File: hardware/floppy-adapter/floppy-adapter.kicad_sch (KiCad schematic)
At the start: 12 parts, among them J1 Conn_02x17 socket (O1 side), J2 Conn_02x17 header (OEM cable), J3 Conn_02x17 header (Gotek), J4 Gotek power, J5 Panel switch, K1 4PDT relay, 5V coil

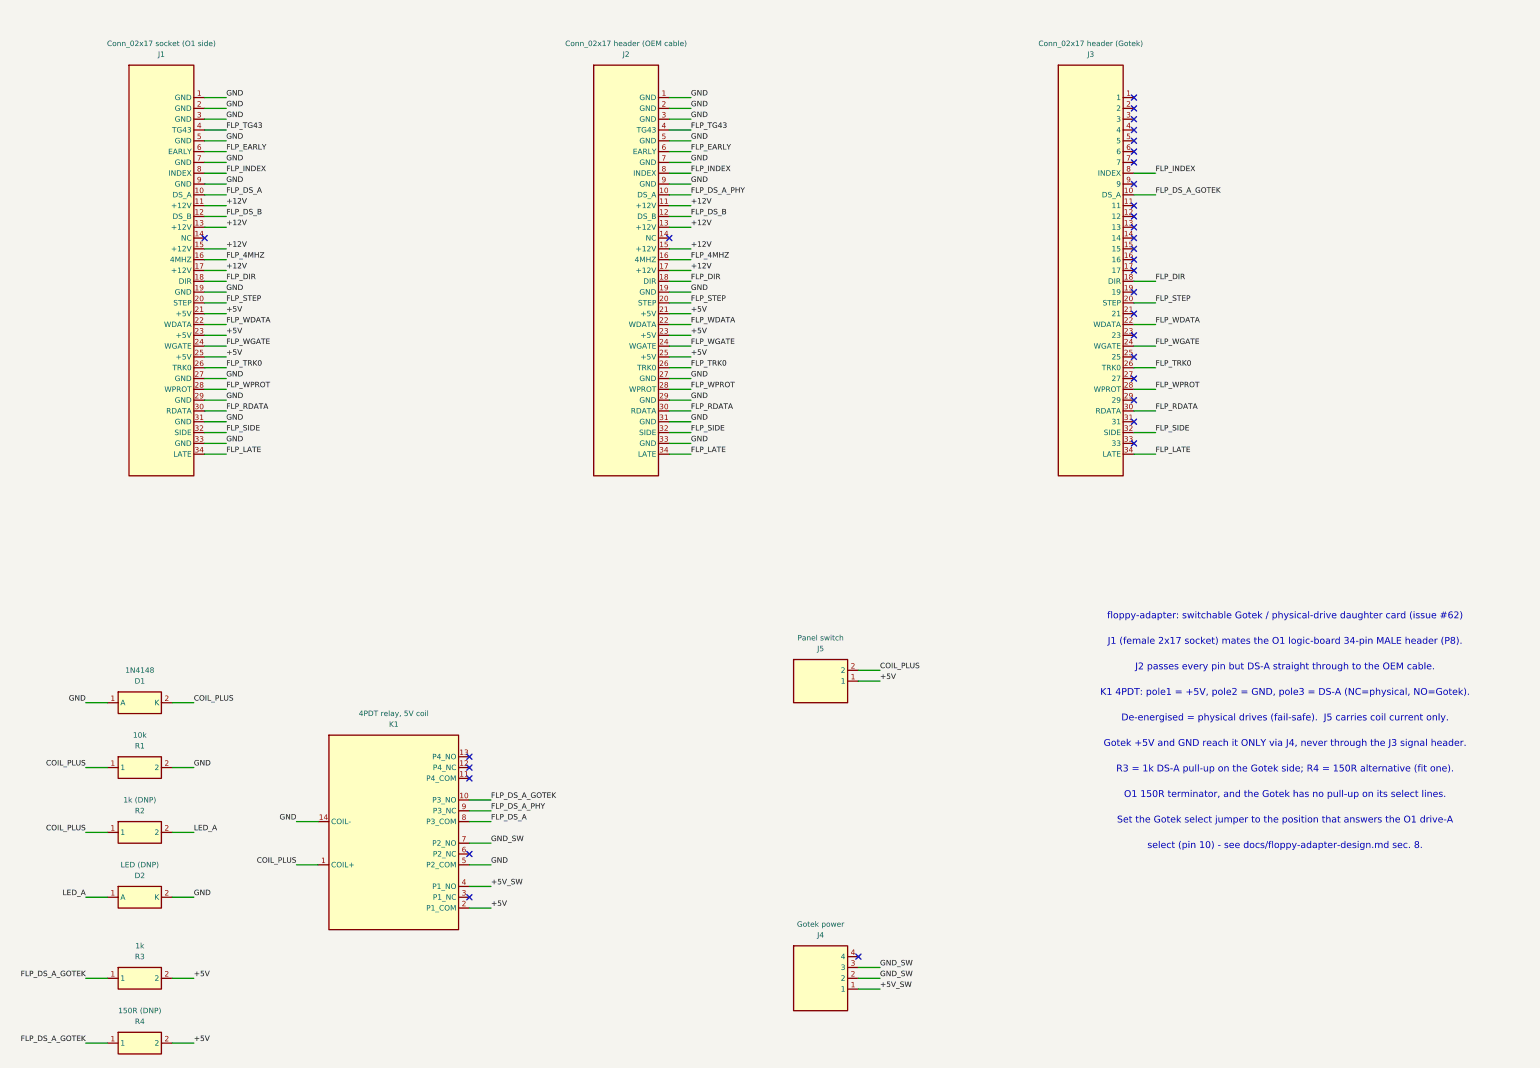
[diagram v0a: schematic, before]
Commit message: hardware: draw the floppy-adapter's nets and give its parts footprints (#62)
The Rev A capture was a net *label* on every pin with no wire between any two
parts: a correct netlist and a drawing nobody could follow.  This is the same
treatment the WiFi COMM PAC got (#347), for the same reasons.

* Every net is routed as orthogonal segments on a 1.27 mm grid by the Manhattan
  A* that `../wifi-comm-pac/gen_wifi_comm_pac_sch.py` uses -- copied, not
  imported, because tools/check_schematics.py regenerates each board's sheet by
  running its generator **alone in a scratch directory**.
* **One label per signal net** (21 of them) keeps the names.  One and not
  fifteen is the safety property: a missing wire breaks the netlist instead of
  being hidden by a label doing the connecting.
* GND/+5V/+12V are routed like signals with **one power symbol each** and a
  PWR_FLAG, not a symbol per pin -- GND lands on eleven pins of J1 and +12V on
  four consecutive ones, and 3.81 mm glyphs 2.54 mm apart stack on top of each
  other.
* **11 of 12 footprints assigned**, from KiCad's own libraries and
  through-hole throughout: this is the board a person builds by hand, and
  `Update PCB from Schematic` transfers nothing for an empty Footprint field.
  K1 is deliberately open (see the next commit): the 4PDT DIP relay class is
  obsolete and a footprint for the wrong package is a board that does not fit.

Two defects came out of it, both found by comparing netlists rather than by
looking at the sheet:

* **A wire ended on a no-connect pin.**  The router blocked other nets' pins
  but not the ones marked no-connect -- they carry no net, so they are not in
  the net-holding table -- and the first wired netlist grew J3.14 and K1.11 onto
  FLP_DS_A_GOTEK.  A no-connect marker says the pin goes nowhere; the netlist
  believes the wire.
* **The checker's floppy pinout table contradicted the design**: it read "pins
  2/4/6 are GND" against sec.2's "pins 4 and 6 are TG43 and EARLY, never
  grou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
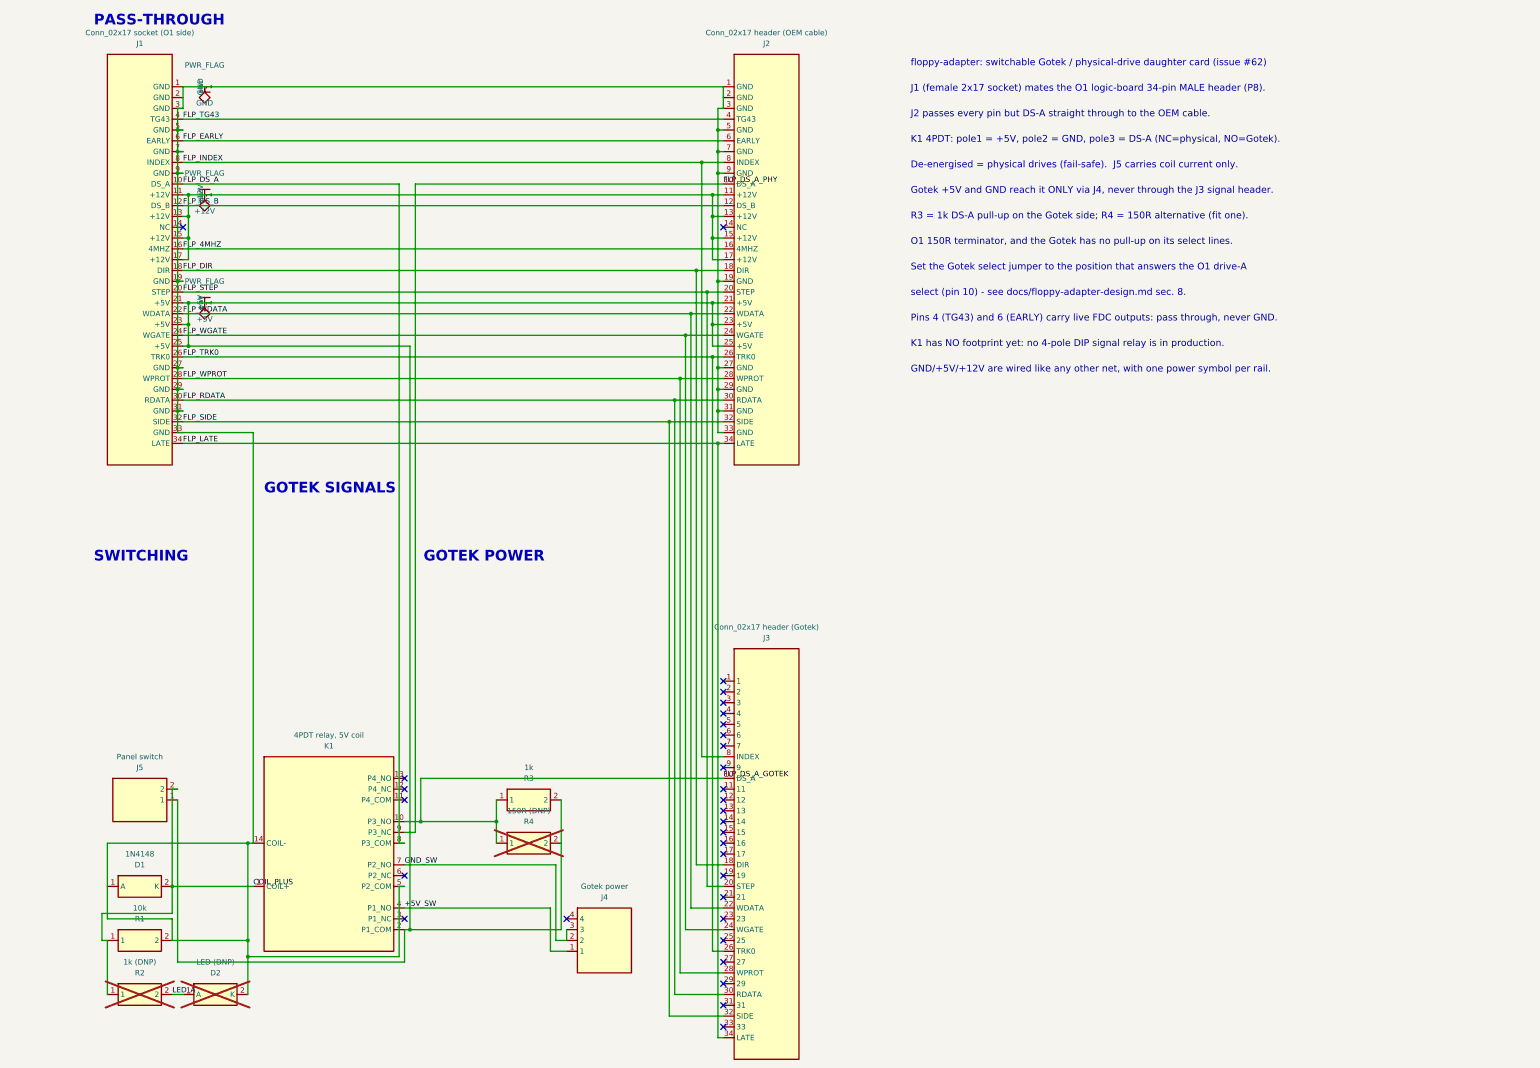
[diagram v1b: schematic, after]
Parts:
- D1: footprint (none) -> Diode_THT:D_DO-35_SOD27_P7.62mm_Horizontal
- D2: footprint (none) -> LED_THT:LED_D5.0mm; now not fitted; now left out of the parts list
- J1: footprint (none) -> Connector_PinSocket_2.54mm:PinSocket_2x17_P2.54mm_Vertical
- J2, J3: footprint (none) -> Connector_IDC:IDC-Header_2x17_P2.54mm_Vertical
- J4: footprint (none) -> Connector_PinHeader_2.54mm:PinHeader_1x04_P2.54mm_Horizontal
- J5: footprint (none) -> Connector_PinHeader_2.54mm:PinHeader_1x02_P2.54mm_Vertical
- R1, R3: footprint (none) -> Resistor_THT:R_Axial_DIN0207_L6.3mm_D2.5mm_P7.62mm_Horizontal
- R2, R4: footprint (none) -> Resistor_THT:R_Axial_DIN0207_L6.3mm_D2.5mm_P7.62mm_Horizontal; now not fitted; now left out of the parts list
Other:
- note added: "GND/+5V/+12V are wired like any other net, with one power symbol per rail."
- note added: "GOTEK POWER"
- note added: "GOTEK SIGNALS"
- note added: "K1 has NO footprint yet: no 4-pole DIP signal relay is in production."
- note added: "PASS-THROUGH"
- note added: "Pins 4 (TG43) and 6 (EARLY) carry live FDC outputs: pass through, never GND."
- note added: "SWITCHING"

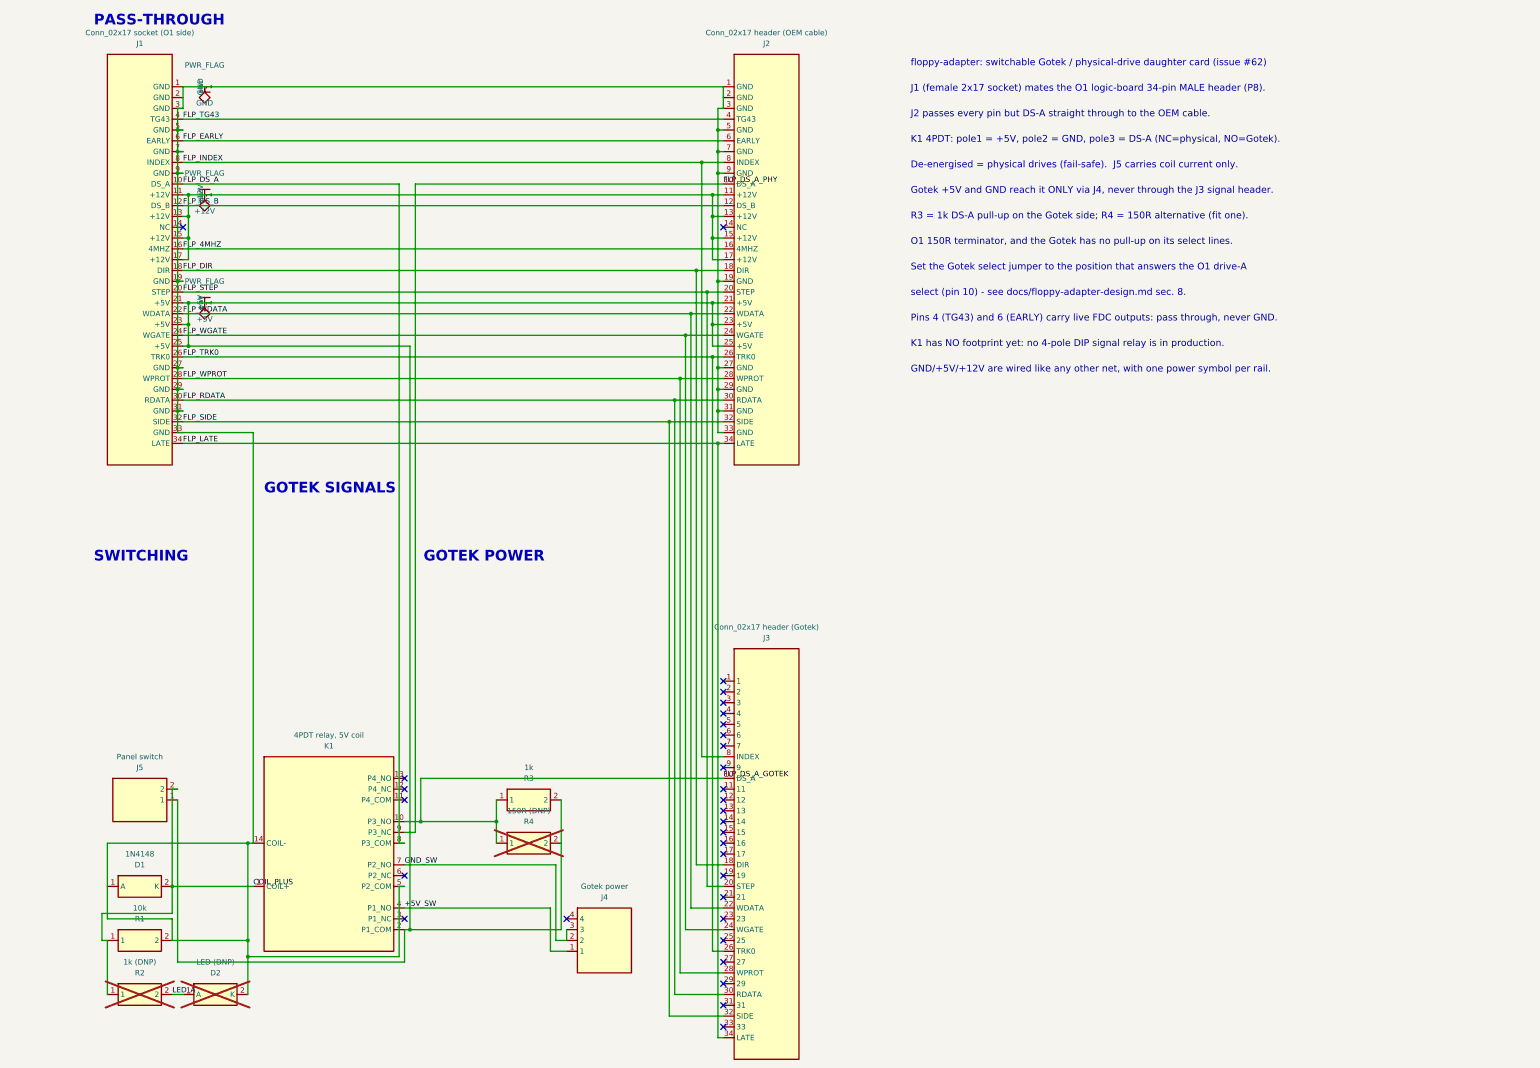
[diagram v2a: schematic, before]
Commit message: hardware: the floppy adapter switches solid state -- no relay, no height (#62)
The maintainer settled the switch question on 2026-10-22, with the constraint the
document never carried: **there is not enough height in the case for relay
blocks.**  A DIP-14 signal relay is ~10 mm and a socketed industrial 4PDT is
35 mm, and this card is a mezzanine between the logic board and the floppy
harness.  So K1 and its coil are gone, and the three switches are silicon:

* **U1 NC7SB3157P6X** (SC70-6) -- DS-A 2:1.  Its own truth table is
  "S low -> B0, S high -> B1", so **B0 is the physical drive**: a low, floating
  or unplugged control parks the machine on the real drive, which is the same
  fail-safe the relay's NC contact gave.  It also has break-before-make, so the
  two devices never share DS-A even momentarily.
* **U2 TPS22918** (SOT-23-6) -- the Gotek's +5 V.  52 mohm, 2 A, logic-level ON;
  CT and QOD left open (open CT is the fastest rise, open QOD disables the
  discharge).
* **Q1 AO3400A** (SOT-23) -- the Gotek's ground return, 28 mohm at Vgs = 4.5 V,
  which is 14 mV at half an amp.  That number is why it is not a second
  PhotoMOS: an AQY212GS is 0.7 ohm, which is 0.35 V of ground offset between the
  Gotek and the machine's TTL signals.

One control node (`CTRL`) drives all three, pulled down by R1 (10k) -- the relay's
coil-node pull-down, kept for the same reason.  D1 (flyback) goes with the coil.
All 13 parts carry a footprint from KiCad's own libraries, and the three switch
symbols use the **parts' own pin numbers**, taken from the datasheets and
cross-checked against KiCad's symbols for them -- which is the thing the relay's
DIP-14 placeholders could never be.

The panel-switch lead now carries microamps instead of 73 mA of coil current.

Checked, not asserted: `kicad-cli sch erc --severity-all` is 0 errors / 19
violations, all 19 the one kind (embedded local: symbols, one per placed symbol);
`kicad-cli sch upgrade` leaves the netlist identical; 0 overlappin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
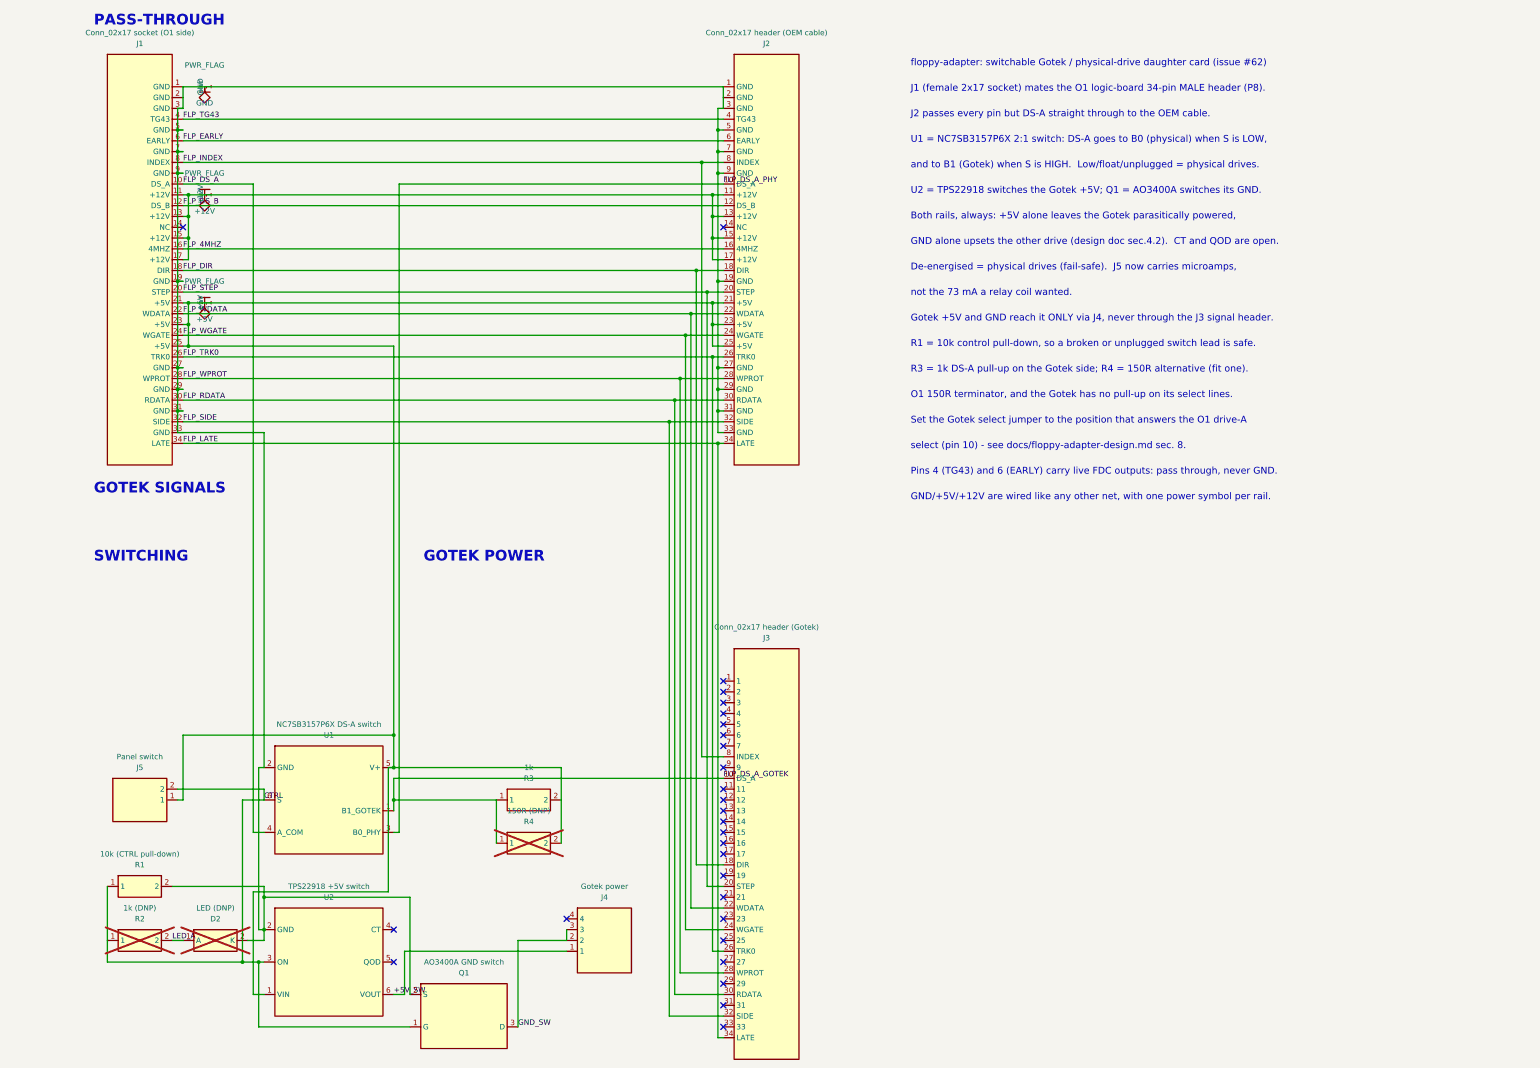
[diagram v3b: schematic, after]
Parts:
- removed D1: 1N4148, Diode_THT:D_DO-35_SOD27_P7.62mm_Horizontal, symbol local:DIODE
- removed K1: 4PDT relay, 5V coil, symbol local:RELAY_4PDT
- added Q1: AO3400A GND switch, Package_TO_SOT_SMD:SOT-23, symbol local:NFET_GSD
- added U1: NC7SB3157P6X DS-A switch, Package_TO_SOT_SMD:SOT-363_SC-70-6, symbol local:BUS_SW_2TO1
- added U2: TPS22918 +5V switch, Package_TO_SOT_SMD:SOT-23-6, symbol local:LOAD_SW
- R1: value 10k -> 10k (CTRL pull-down)
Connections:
- net +5V: now also U1.5 (V+), U2.1 (VIN)
- net +5V_SW: now also U2.6 (VOUT)
- net FLP_DS_A: now also U1.4 (A_COM)
- net FLP_DS_A_GOTEK: now also U1.1 (B1_GOTEK)
- net FLP_DS_A_PHY: now also U1.3 (B0_PHY)
- net GND: now also Q1.2 (S), U1.2 (GND), U2.2 (GND)
- net GND_SW: now also Q1.3 (D)
- net COIL_PLUS renamed CTRL
- net CTRL: now also Q1.1 (G), U1.6 (S), U2.3 (ON)
- no-connect marks 31 -> 28
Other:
- note added: "Both rails, always: +5V alone leaves the Gotek parasitically powered,"
- note added: "De-energised = physical drives (fail-safe). J5 now carries microamps,"
- note added: "GND alone upsets the other drive (design doc sec.4.2). CT and QOD are open."
- note added: "R1 = 10k control pull-down, so a broken or unplugged switch lead is safe."
- note added: "U1 = NC7SB3157P6X 2:1 switch: DS-A goes to B0 (physical) when S is LOW,"
- note added: "U2 = TPS22918 switches the Gotek +5V; Q1 = AO3400A switches its GND."
- note added: "and to B1 (Gotek) when S is HIGH. Low/float/unplugged = physical drives."
- note added: "not the 73 mA a relay coil wanted."
- note removed: "De-energised = physical drives (fail-safe). J5 carries coil current only."
- note removed: "K1 4PDT: pole1 = +5V, pole2 = GND, pole3 = DS-A (NC=physical, NO=Gotek)."
- note removed: "K1 has NO footprint yet: no 4-pole DIP signal relay is in production."
